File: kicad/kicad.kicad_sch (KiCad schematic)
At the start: 107 parts, among them J1 Conn_01x16_Pin, K0 !,,,,,,1, K1 ",,,,,,2, K10 *,,,,,,:, K11 =,,,,,,-, K12 Break, K13 Up, K14 Q, K15 W, K16 E, K17 R, K18 T, K19 Y, K2 #,,,,,,3, K20 U, K21 I, K22 O, K23 P, K24 @, K25 Left, K26 Right, K27 Down, K28 A, K29 S, K3 $,,,,,,4, K30 D, K31 F, K32 G, K33 H, K34 J, K35 K, K36 L, K37 +,,,,,,;, K38 ENTER, K39 CLEAR, K4 %,,,,,,5, K40 SHIFT, K41 Z, K42 X, K43 C, K44 V, K45 B, K46 N, K47 M, K48 <,,,,,,,, K49 >,,,,,,., K5 &,,,,,,6, K50 ?,,,,,,/, K51 SHIFT, K52 Blank, K6 ',,,,,,7, K7 (,,,,,,8, K8 ),,,,,,9, K9 0

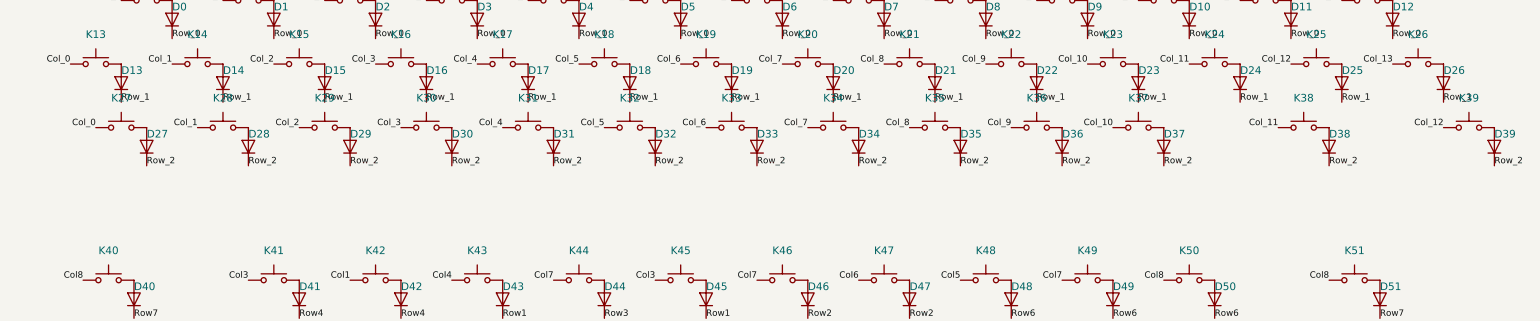
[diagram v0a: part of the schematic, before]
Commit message: More rows, needs double-check
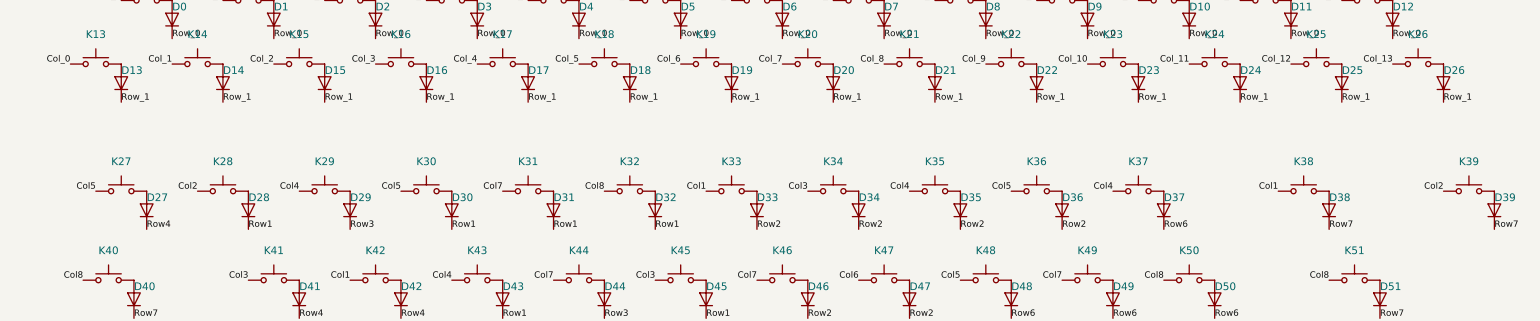
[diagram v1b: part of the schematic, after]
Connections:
- net Col1: now also K33.1, K38.1
- net Col2: now also K28.1, K39.1
- net Col3: now also K34.1
- net Col4: now also K29.1, K35.1, K37.1
- net Col5: now also K27.1, K30.1, K36.1
- net Col7: now also K31.1
- net Col8: now also K32.1
- net Col_0: no longer K27.1
- net Col_1: no longer K28.1
- net Col_10: no longer K37.1
- net Col_11: no longer K38.1
- net Col_12: no longer K39.1
- net Col_2: no longer K29.1
- net Col_3: no longer K30.1
- net Col_4: no longer K31.1
- net Col_5: no longer K32.1
- net Col_6: no longer K33.1
- net Col_7: no longer K34.1
- net Col_8: no longer K35.1
- net Col_9: no longer K36.1
- net Row1: now also D28.1 (K), D30.1 (K), D31.1 (K), D32.1 (K)
- net Row2: now also D33.1 (K), D34.1 (K), D35.1 (K), D36.1 (K)
- net Row3: now also D29.1 (K)
- net Row4: now also D27.1 (K)
- net Row6: now also D37.1 (K)
- net Row7: now also D38.1 (K), D39.1 (K)
- removed net Row_2: D27.1 (K), D28.1 (K), D29.1 (K), D30.1 (K), D31.1 (K), D32.1 (K), D33.1 (K), D34.1 (K), D35.1 (K), D36.1 (K), D37.1 (K), D38.1 (K), D39.1 (K)
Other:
- moved on the sheet: D27, D28, D29, D30, D31, D32, D33, D34, D35, D36, D37, D38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

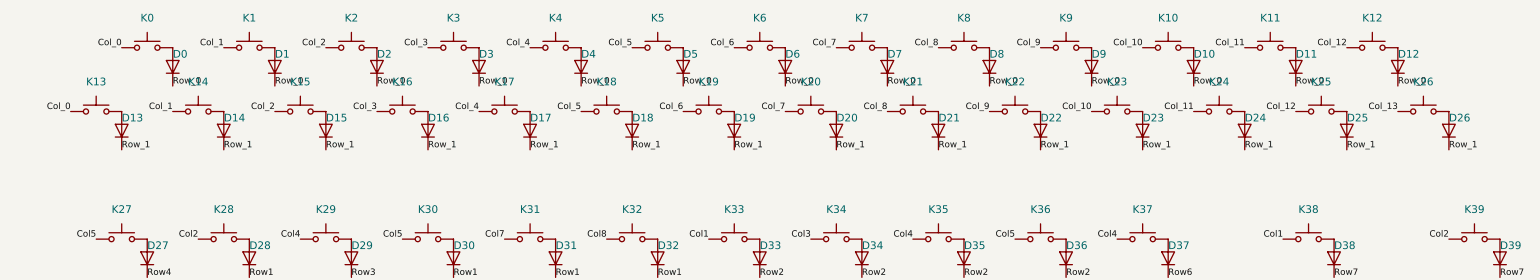
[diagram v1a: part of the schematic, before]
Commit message: Matrix laid out
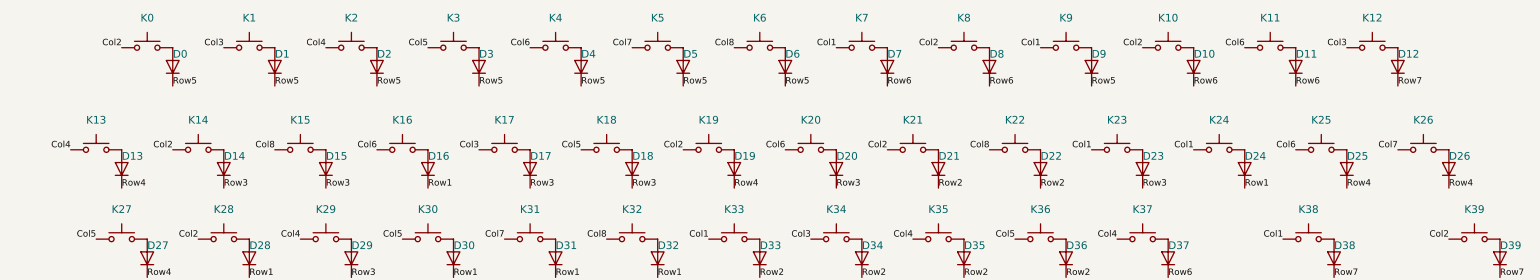
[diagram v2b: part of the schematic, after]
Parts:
- J1: footprint (none) -> Connector_PinSocket_2.54mm:PinSocket_1x16_P2.54mm_Horizontal
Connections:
- net Col_13 is gone; now on net Col7: K26.1
- net Col_8 is gone; now on net Col2: K21.1, K8.1
- net Col1: now also K23.1, K24.1, K7.1, K9.1
- net Col2: now also K0.1, K10.1, K14.1, K19.1
- net Col3: now also K1.1, K12.1, K17.1
- net Col4: now also K13.1, K2.1
- net Col5: now also K18.1, K3.1
- net Col6: now also K11.1, K16.1, K20.1, K25.1, K4.1
- net Col7: now also K5.1
- net Col8: now also K15.1, K22.1, K6.1
- net Row1: now also D16.1 (K), D24.1 (K)
- net Row2: now also D21.1 (K), D22.1 (K)
- net Row3: now also D14.1 (K), D15.1 (K), D17.1 (K), D18.1 (K), D20.1 (K), D23.1 (K)
- net Row4: now also D13.1 (K), D19.1 (K), D25.1 (K), D26.1 (K)
- net Row5: now also D0.1 (K), D1.1 (K), D2.1 (K), D3.1 (K), D4.1 (K), D5.1 (K), D6.1 (K), D9.1 (K)
- net Row6: now also D10.1 (K), D11.1 (K), D7.1 (K), D8.1 (K)
- net Row7: now also D12.1 (K)
- removed net Col_0: K0.1, K13.1
- removed net Col_1: K1.1, K14.1
- removed net Col_10: K10.1, K23.1
- removed net Col_11: K11.1, K24.1
- removed net Col_12: K12.1, K25.1
- removed net Col_2: K15.1, K2.1
- removed net Col_3: K16.1, K3.1
- removed net Col_4: K17.1, K4.1
- removed net Col_5: K18.1, K5.1
- removed net Col_6: K19.1, K6.1
- removed net Col_7: K20.1, K7.1
- removed net Col_9: K22.1, K9.1
- removed net Row_0: D0.1 (K), D1.1 (K), D10.1 (K), D11.1 (K), D12.1 (K), D2.1 (K), D3.1 (K), D4.1 (K), D5.1 (K), D6.1 (K), D7.1 (K), D8.1 (K), D9.1 (K)
- removed net Row_1: D13.1 (K), D14.1 (K), D15.1 (K), D16.1 (K), D17.1 (K), D18.1 (K), D19.1 (K), D20.1 (K), D21.1 (K), D22.1 (K), D23.1 (K), D24.1 (K), D25.1 (K), D26.1 (K)
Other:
- moved on the sheet: D13, D14, D15, D16, D17, D18, D19, D20, D21, D22, D23, D24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

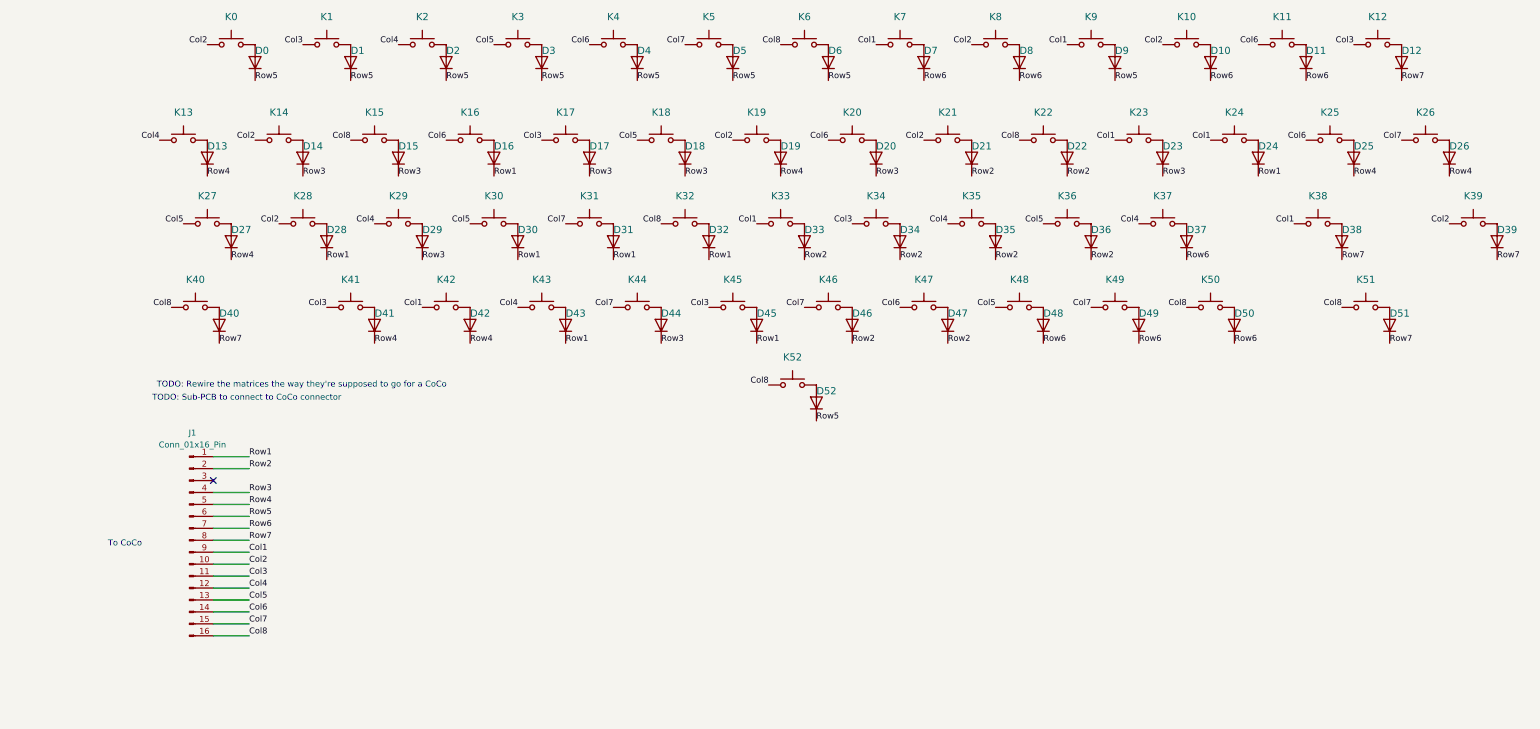
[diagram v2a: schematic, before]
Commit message: Diodes removed, mounts added
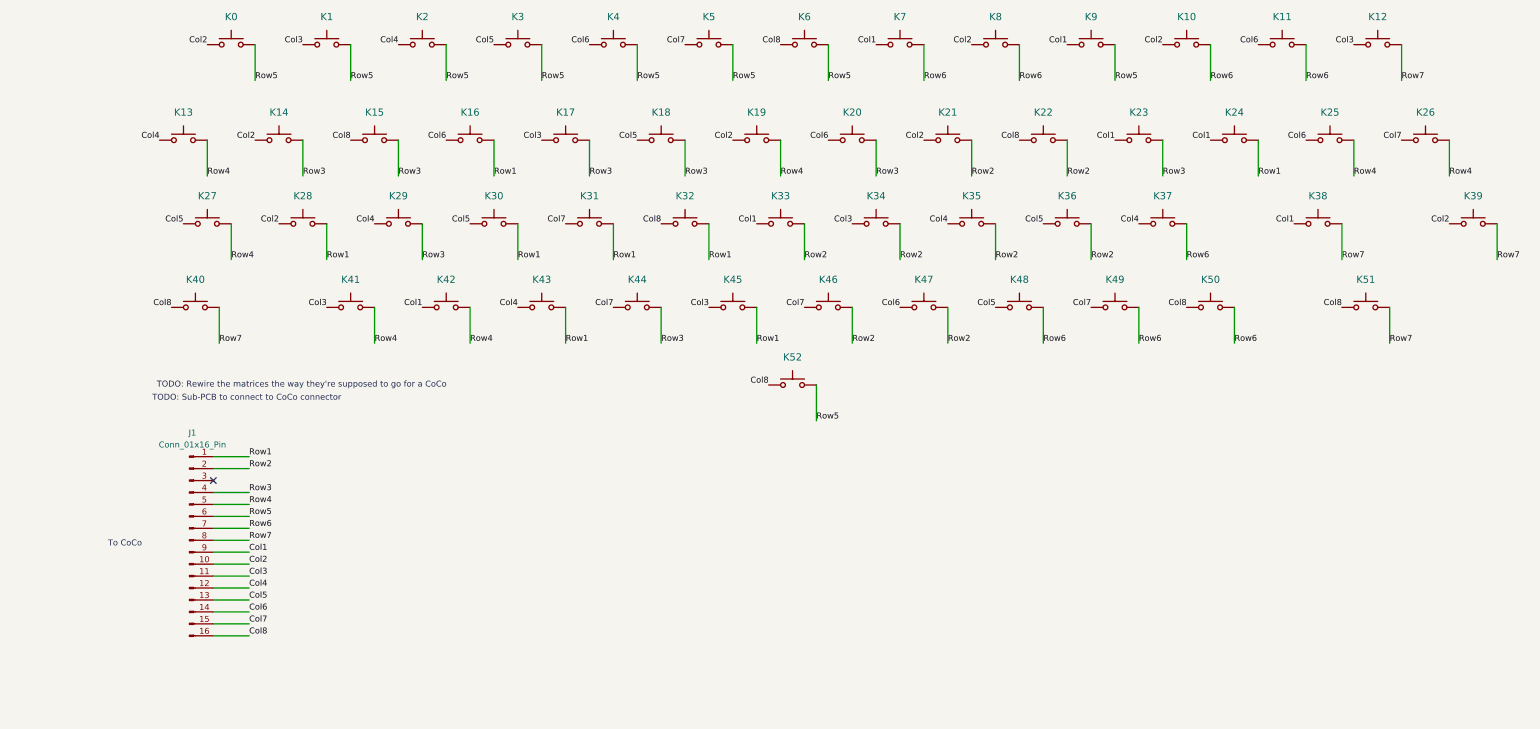
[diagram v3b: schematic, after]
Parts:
- removed D0, D1, D10, D11, D12, D13, D14, D15, D16, D17, D18, D19, D2, D20, D21, D22, D23, D24, D25, D26, D27, D28, D29, D3, D30, D31, D32, D33, D34, D35, D36, D37, D38, D39, D4, D40, D41, D42, D43, D44, D45, D46, D47, D48, D49, D5, D50, D51, D52, D6, D7, D8, D9: D, Diode_SMD:D_0805_2012Metric_Pad1.15x1.40mm_HandSolder, symbol Device:D
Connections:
- net Row1: now also K16.2, K24.2, K28.2, K30.2, K31.2, K32.2, K43.2, K45.2
- net Row2: now also K21.2, K22.2, K33.2, K34.2, K35.2, K36.2, K46.2, K47.2
- net Row3: now also K14.2, K15.2, K17.2, K18.2, K20.2, K23.2, K29.2, K44.2
- net Row4: now also K13.2, K19.2, K25.2, K26.2, K27.2, K41.2, K42.2
- net Row5: now also K0.2, K1.2, K2.2, K3.2, K4.2, K5.2, K52.2, K6.2, K9.2
- net Row6: now also K10.2, K11.2, K37.2, K48.2, K49.2, K50.2, K7.2, K8.2
- net Row7: now also K12.2, K38.2, K39.2, K40.2, K51.2

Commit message: Routed
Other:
- note added: "TODO: Get the connector right"
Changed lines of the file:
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@@
+		)
+	)
+	(text "TODO: Get the connector right"
+		(exclude_from_sim no)
+		(at 21.59 145.288 0)
+		(effects
+			(font
+				(size 1.27 1.27)
+			)
 		)
 	)

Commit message: TODOs
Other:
- note added: "TODO: Mounting holes for plate, if we decide we need one"
- note added: "TODO: Overall mounting holes"
- note removed: "TODO: Rewire the matrices the way they're supposed to go for a CoCo"
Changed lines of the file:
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@@
+		)
+	)
+	(text "TODO: Overall mounting holes"
+		(exclude_from_sim no)
+		(at 41.91 106.934 0)
+		(effects
+			(font
+				(size 1.27 1.27)
+			)
 		)
 	)
@@
 		)
 	)
-	(text "TODO: Rewire the matrices the way they're supposed to go for a CoCo"
+	(text "TODO: Mounting holes for plate, if we decide we need one"
 		(exclude_from_sim no)
-		(at 65.786 99.06 0)
+		(at 43.434 104.394 0)
 		(effects
 			(font

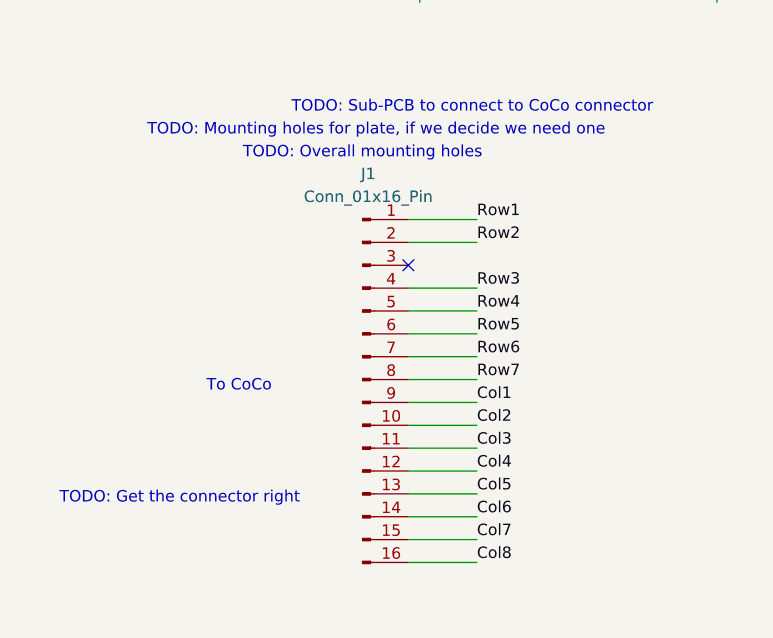
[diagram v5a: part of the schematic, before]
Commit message: Routed in the connector, although I need to double check
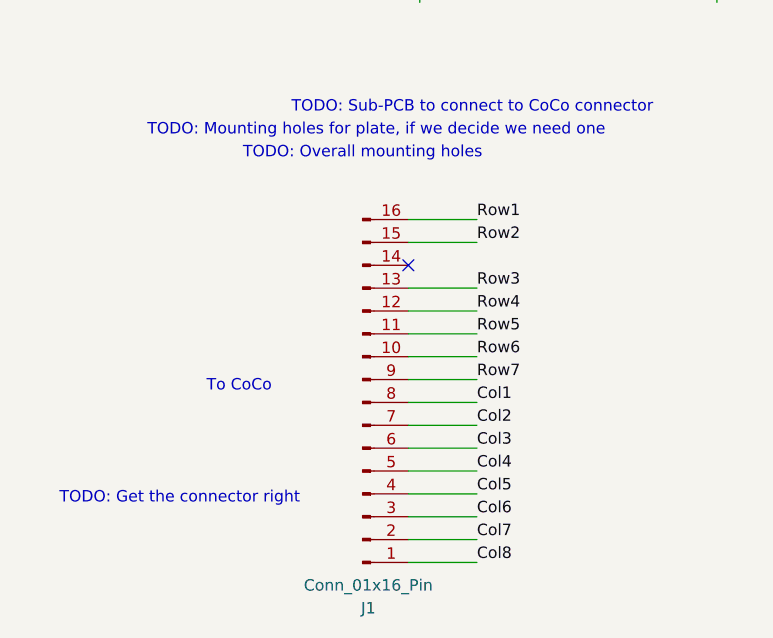
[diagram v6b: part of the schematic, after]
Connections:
- net Col1: now also J1.8 (Pin_8); no longer J1.9 (Pin_9)
- net Col2: now also J1.7 (Pin_7); no longer J1.10 (Pin_10)
- net Col3: now also J1.6 (Pin_6); no longer J1.11 (Pin_11)
- net Col4: now also J1.5 (Pin_5); no longer J1.12 (Pin_12)
- net Col5: now also J1.4 (Pin_4); no longer J1.13 (Pin_13)
- net Col6: now also J1.3 (Pin_3); no longer J1.14 (Pin_14)
- net Col7: now also J1.2 (Pin_2); no longer J1.15 (Pin_15)
- net Col8: now also J1.1 (Pin_1); no longer J1.16 (Pin_16)
- net Row1: now also J1.16 (Pin_16); no longer J1.1 (Pin_1)
- net Row2: now also J1.15 (Pin_15); no longer J1.2 (Pin_2)
- net Row3: now also J1.13 (Pin_13); no longer J1.4 (Pin_4)
- net Row4: now also J1.12 (Pin_12); no longer J1.5 (Pin_5)
- net Row5: now also J1.11 (Pin_11); no longer J1.6 (Pin_6)
- net Row6: now also J1.10 (Pin_10); no longer J1.7 (Pin_7)
- net Row7: now also J1.9 (Pin_9); no longer J1.8 (Pin_8)

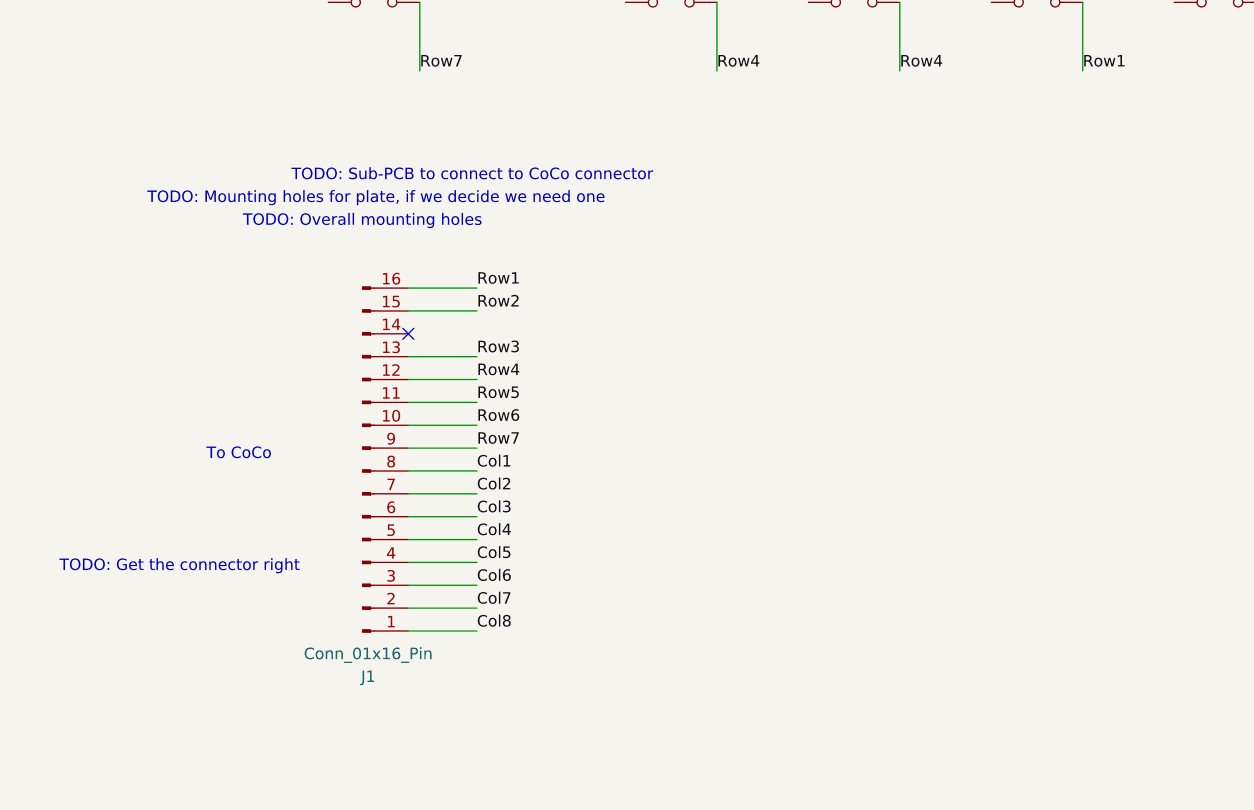
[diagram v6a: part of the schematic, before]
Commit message: Add F-board pull-up
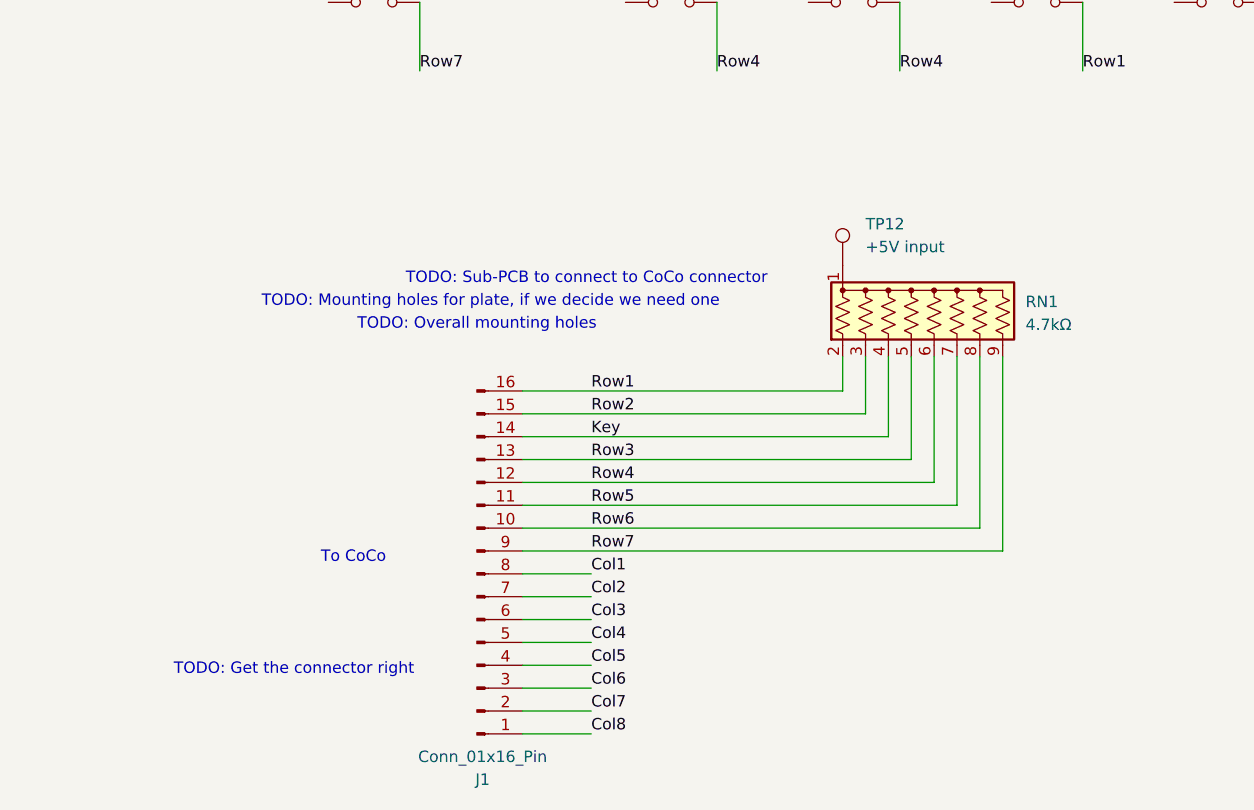
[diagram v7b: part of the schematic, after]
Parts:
- added RN1: 4.7kΩ, Resistor_THT:R_Array_SIP9, symbol Device:R_Network08_US
- added TP12: +5V input, Connector_PinHeader_2.54mm:PinHeader_1x01_P2.54mm_Horizontal, symbol Connector:TestPoint
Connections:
- net Row1: now also RN1.2 (R1)
- net Row2: now also RN1.3 (R2)
- net Row3: now also RN1.5 (R4)
- net Row4: now also RN1.6 (R5)
- net Row5: now also RN1.7 (R6)
- net Row6: now also RN1.8 (R7)
- net Row7: now also RN1.9 (R8)
- net Key: now reaches J1.14 (Pin_14)
- net Key: now also RN1.4 (R3)
- new net: RN1.1 (common), TP12.1
- no-connect marks 1 -> 0
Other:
- moved on the sheet: J1

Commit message: Fix Spacebar
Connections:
- net Row4: now also K52.2
- net Row5: no longer K52.2
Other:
- note added: "Bodge list: - Space bar should be on row 4"
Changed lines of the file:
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@@
+		)
+	)
+	(text "Bodge list:\n- Space bar should be on row 4"
+		(exclude_from_sim no)
+		(at 175.768 116.586 0)
+		(effects
+			(font
+				(size 1.27 1.27)
+			)
+			(justify left)
 		)
 	)
@@
 		)
 	)
-	(label "Row5"
+	(label "Row4"
 		(at 175.26 106.68 0)
 		(fields_autoplaced yes)
